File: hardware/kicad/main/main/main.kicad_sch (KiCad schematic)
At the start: 7 parts, among them J1 USB_C_Receptacle_USB2.0, J2 SERVO_L, J3 SERVO_R, U1 CH340G, U2 ESP32-WROOM-32

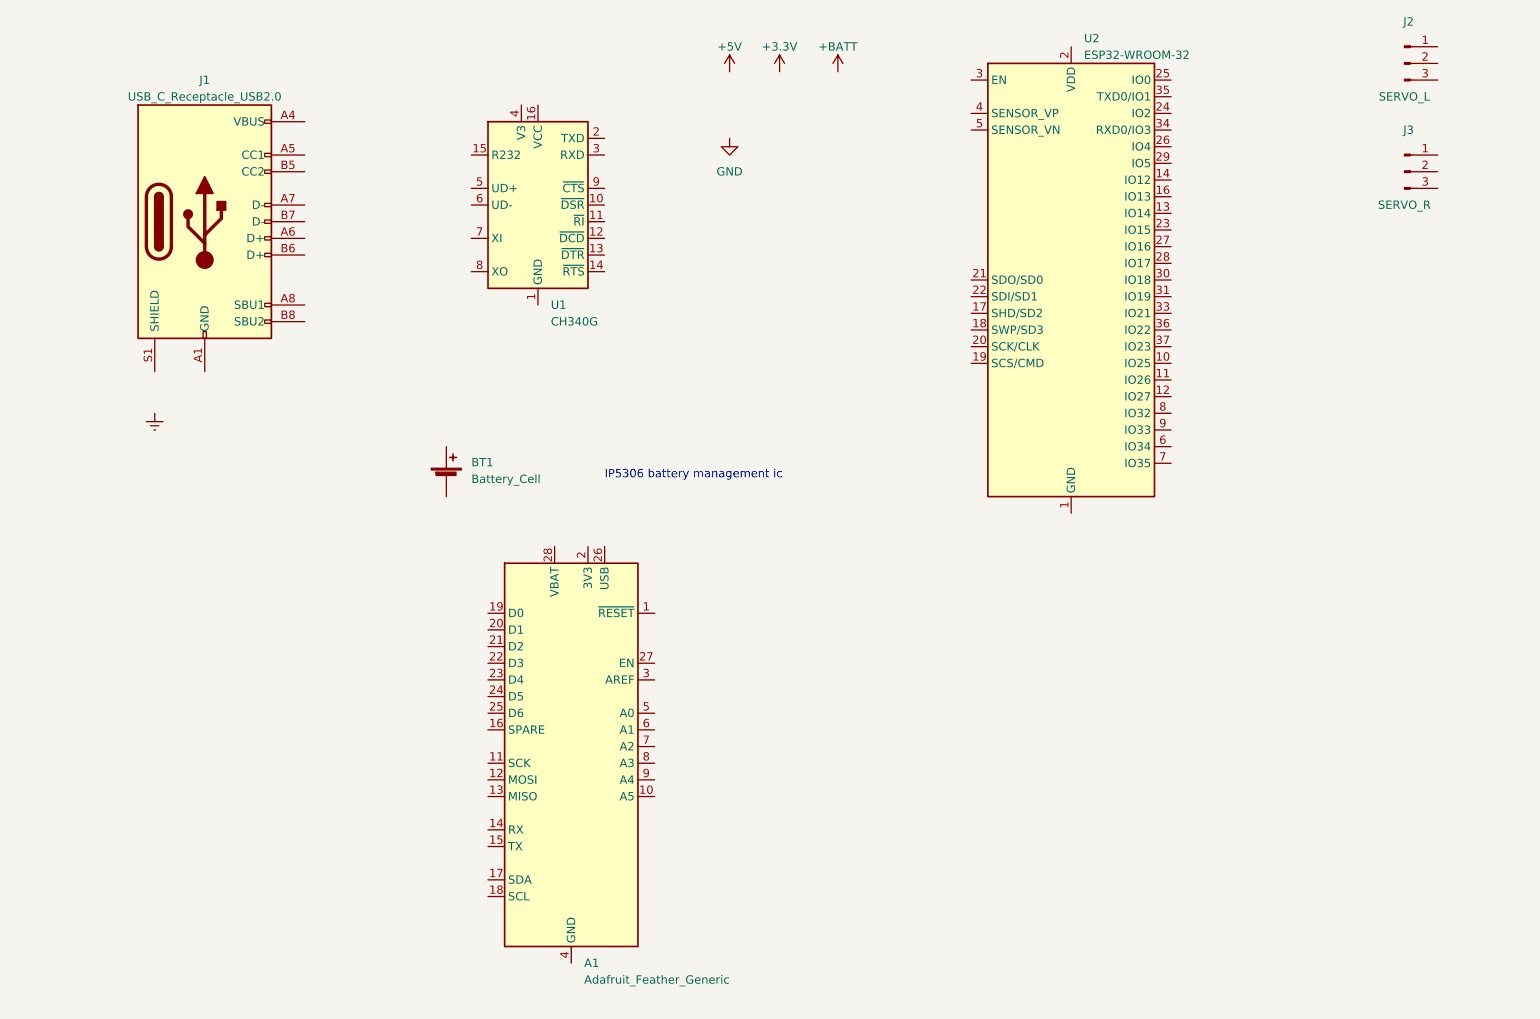
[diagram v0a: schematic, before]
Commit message: added battery charging ic, mounting holes
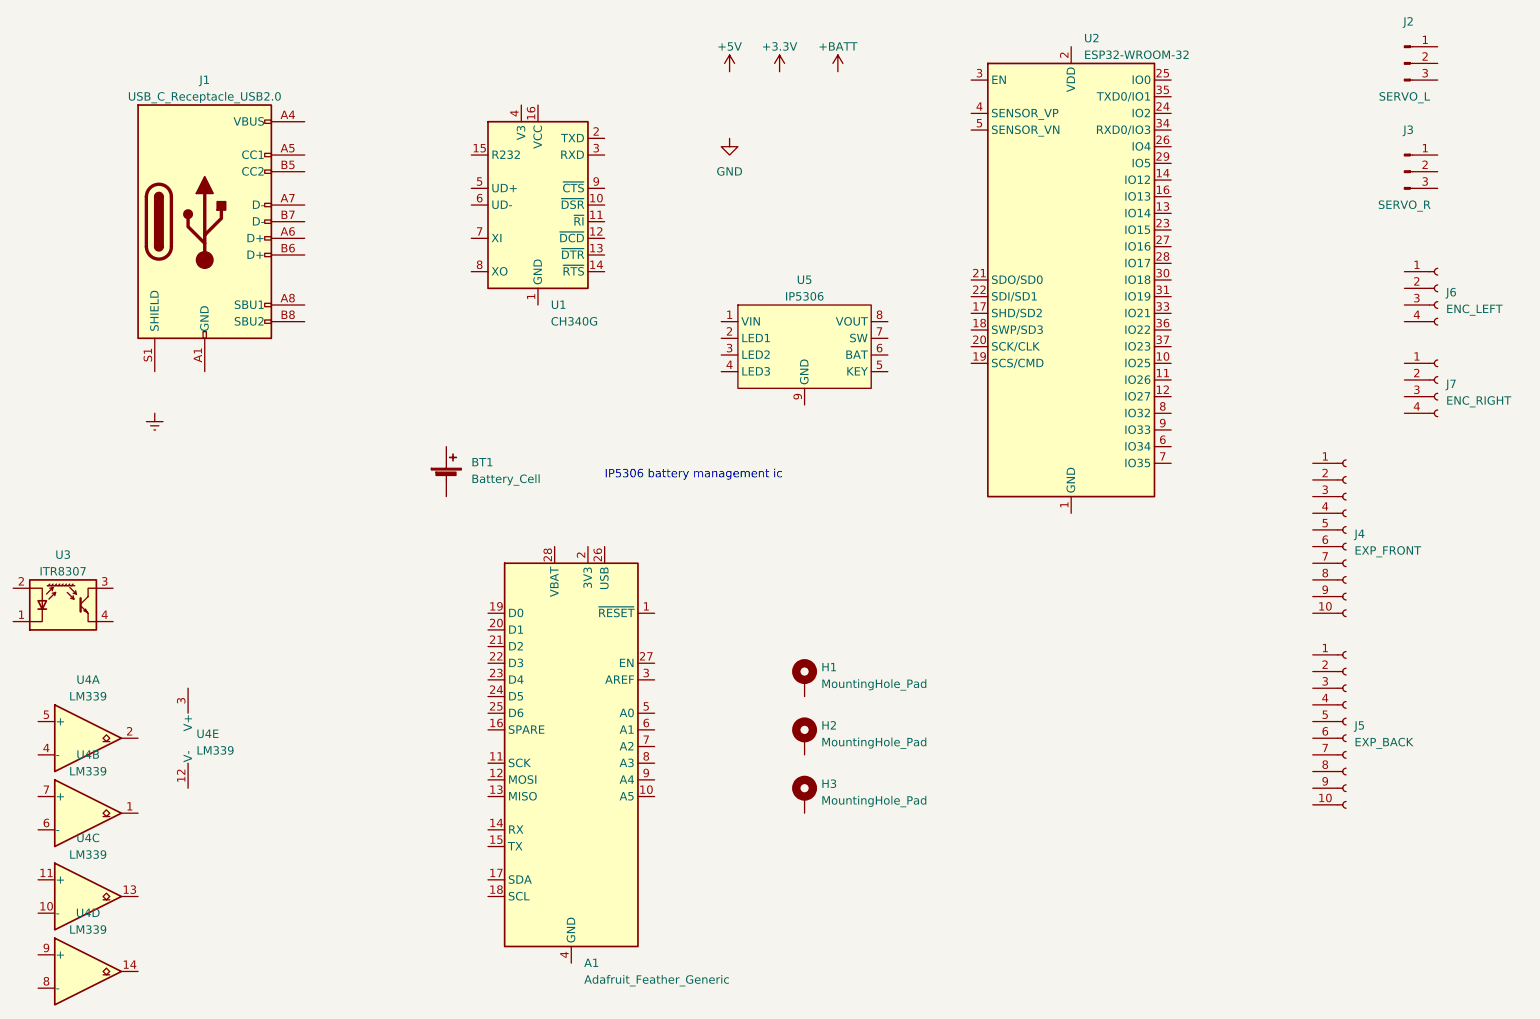
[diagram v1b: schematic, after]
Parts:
- added H1, H2, H3: MountingHole_Pad, MountingHole:MountingHole_3.2mm_M3_DIN965_Pad, symbol Mechanical:MountingHole_Pad
- added J4: EXP_FRONT, Connector_PinSocket_2.54mm:PinSocket_1x10_P2.54mm_Horizontal, symbol Connector:Conn_01x10_Socket
- added J5: EXP_BACK, Connector_PinSocket_2.54mm:PinSocket_1x10_P2.54mm_Horizontal, symbol Connector:Conn_01x10_Socket
- added J6: ENC_LEFT, Connector_PinSocket_2.54mm:PinSocket_1x04_P2.54mm_Horizontal, symbol Connector:Conn_01x04_Socket
- added J7: ENC_RIGHT, Connector_PinSocket_2.54mm:PinSocket_1x04_P2.54mm_Horizontal, symbol Connector:Conn_01x04_Socket
- added U3: ITR8307, OptoDevice:Everlight_ITR8307, symbol Sensor_Proximity:ITR8307
- added U4: LM339, Package_SO:SOIC-14_3.9x8.7mm_P1.27mm, symbol Comparator:LM339
- added U5: IP5306, Package_SO:Diodes_SO-8EP, symbol JLC:IP5306
- BT1: footprint (none) -> Battery:BatteryHolder_MPD_BH-18650-PC2
- J2, J3: footprint (none) -> Connector_PinHeader_2.54mm:PinHeader_1x03_P2.54mm_Horizontal
